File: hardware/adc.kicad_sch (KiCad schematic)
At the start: 15 parts, among them U2 MCP3562R-E/ST

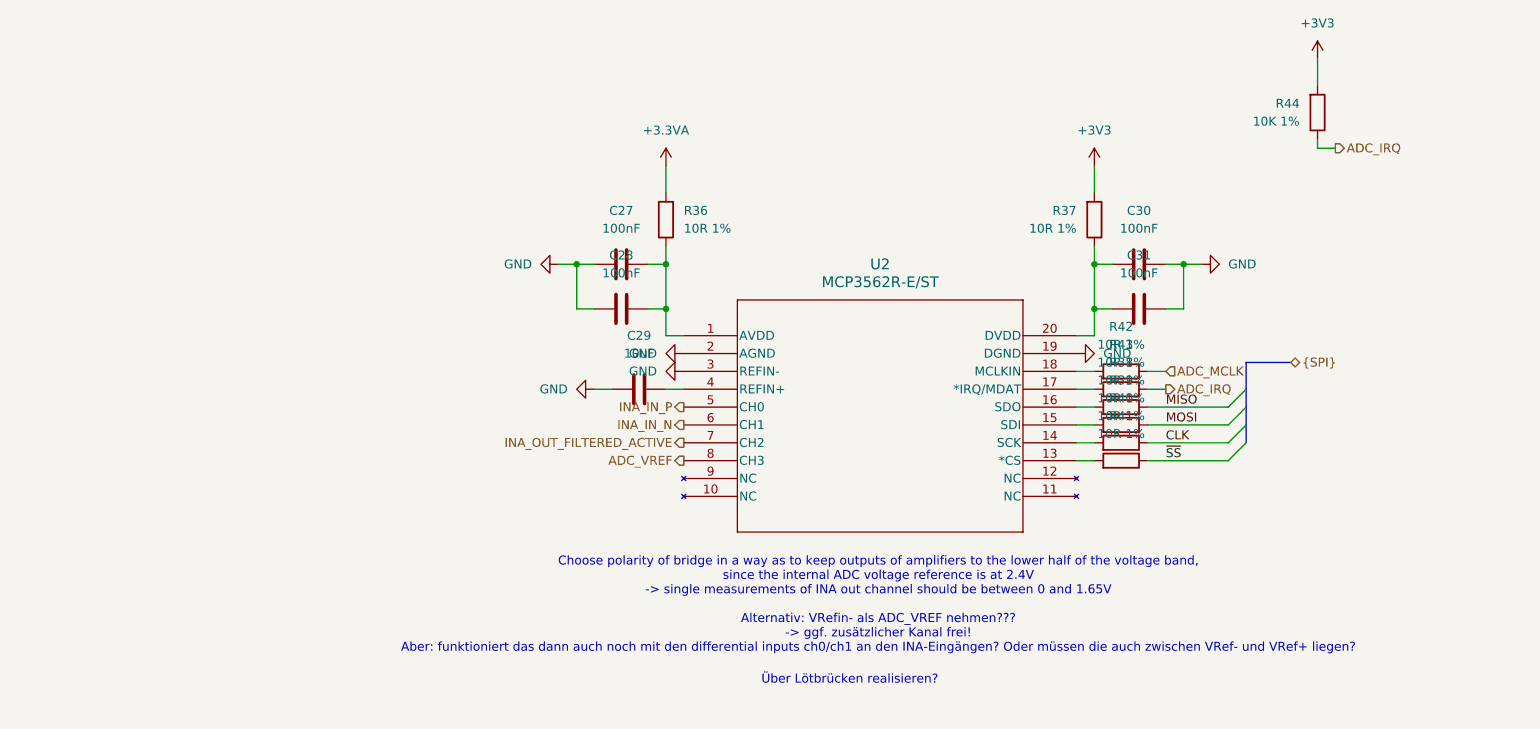
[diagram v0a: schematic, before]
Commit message: Added solder bridges and calculated resistor values for INA
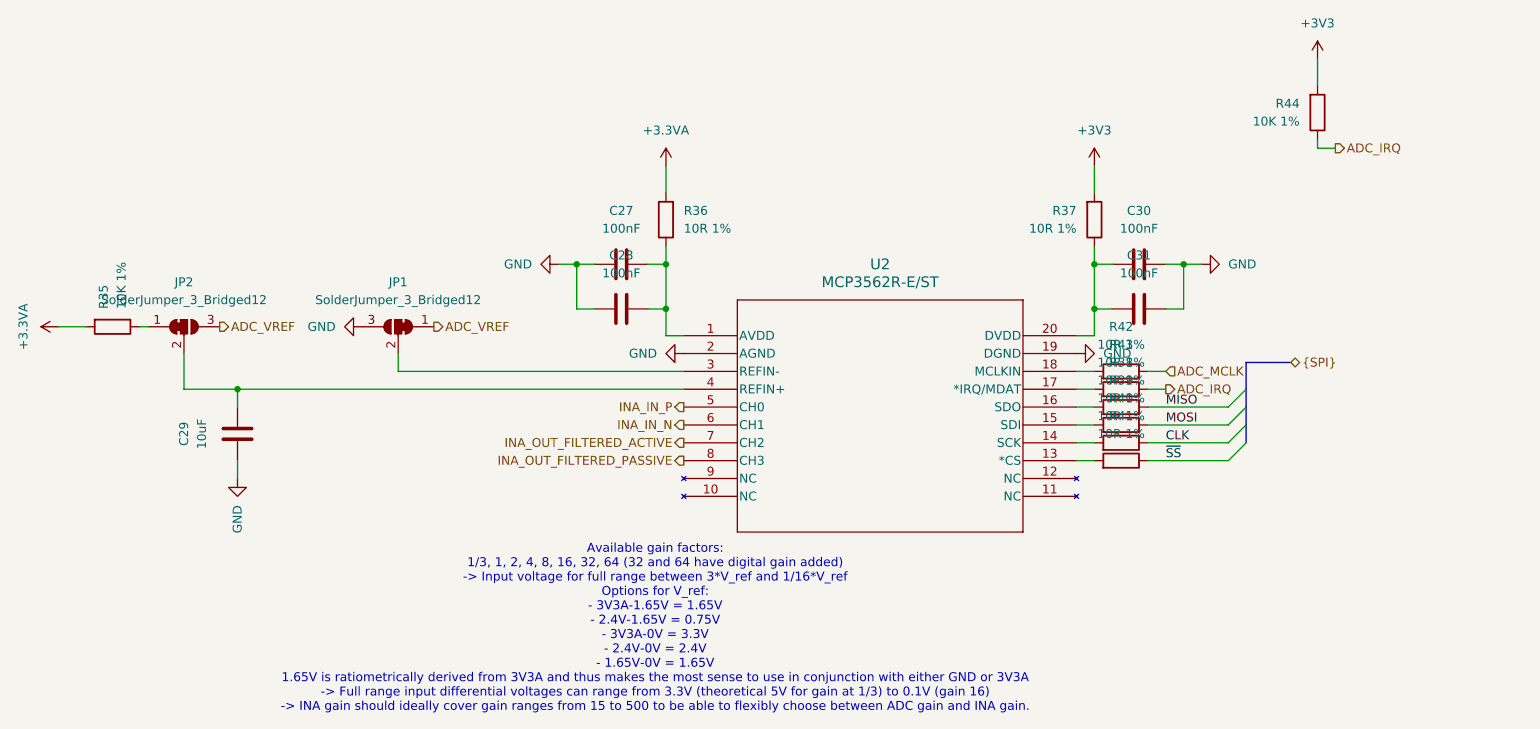
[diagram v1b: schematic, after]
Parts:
- added JP1, JP2: SolderJumper_3_Bridged12, symbol Jumper:SolderJumper_3_Bridged12
- added R35: 10K 1%, Resistor_SMD:R_0603_1608Metric, symbol Device:R
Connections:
- net +3.3VA: now also R35.2
- net ADC_VREF: now also JP1.1 (A), JP2.3 (B); no longer U2.8 (CH3)
- net GND: now also JP1.3 (B); no longer U2.3 (REFIN-)
- net at C29.2, U2.4 (REFIN+): now also JP2.2 (C)
- new net: JP2.1 (A), R35.1
- new net: JP1.2 (C), U2.3 (REFIN-)
- new net INA_OUT_FILTERED_PASSIVE: U2.8 (CH3)
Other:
- note added: "Available gain factors: 1/3, 1, 2, 4, 8, 16, 32, 64 (32 and 64 have digital gain added) -> Input voltage for full range between 3*V_ref and 1/16*V_ref Options for V_ref: - 3V3A-1.65V = 1.65V - 2.4V-1.65V = 0.75V - 3V3A-0V = 3.3V - 2.4V-0V = 2.4V - 1.65V-0V = 1.65V 1.65V is ratiometrically derived from 3V3A and thus makes the most sense to use in conjunction with either GND or 3V3A -> Full range i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"
- note removed: "Choose polarity of bridge in a way as to keep outputs of amplifiers to the lower half of the voltage band, since the internal ADC voltage reference is at 2.4V -> single measurements of INA out channel should be between 0 and 1.65V Alternativ: VRefin- als ADC_VREF nehmen??? -> ggf. zusätzlicher Kanal frei! Aber: funktioniert das dann auch noch mit den differential inputs ch0/ch1 an den INA-Eingäng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"
- note removed: "Über Lötbrücken realisieren?"
- moved on the sheet: C29

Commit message: Set jumper footprints and updated design rules for Oshpark After Dark
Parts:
- JP1, JP2: footprint (none) -> Jumper:SolderJumper-3_P1.3mm_Bridged2Bar12_RoundedPad1.0x1.5mm
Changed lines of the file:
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@@
 			)
 		)
-		(property "Footprint" ""
+		(property "Footprint" "Jumper:SolderJumper-3_P1.3mm_Bridged2Bar12_RoundedPad1.0x1.5mm"
 			(at 36.83 87.63 0)
 			(effects
@@
 			)
 		)
-		(property "Footprint" ""
+		(property "Footprint" "Jumper:SolderJumper-3_P1.3mm_Bridged2Bar12_RoundedPad1.0x1.5mm"
 			(at 67.31 87.63 0)
 			(effects

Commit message: Added net classes
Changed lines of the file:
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@@
+		)
+	)
+	(wire
+		(pts
+			(xy 99.06 101.6) (xy 107.95 101.6)
+		)
+		(stroke
+			(width 0)
+			(type default)
+		)
+	)
+	(wire
+		(pts
+			(xy 99.06 106.68) (xy 107.95 106.68)
+		)
+		(stroke
+			(width 0)
+			(type default)
 		)
 	)
@@
 	(wire
 		(pts
+			(xy 99.06 99.06) (xy 107.95 99.06)
+		)
+		(stroke
+			(width 0)
+			(type default)
+		)
+	)
+	(wire
+		(pts
 			(xy 173.99 99.06) (xy 185.42 99.06)
 		)
@@
 		(pts
 			(xy 166.37 78.74) (xy 166.37 85.09)
+		)
+		(stroke
+			(width 0)
+			(type default)
+		)
+	)
+	(wire
+		(pts
+			(xy 99.06 104.14) (xy 107.95 104.14)
 		)
 		(stroke
@@
 	(hierarchical_label "INA_OUT_FILTERED_PASSIVE"
 		(shape output)
-		(at 107.95 106.68 180)
+		(at 99.06 106.68 180)
 		(effects
 			(font
@@
 	(hierarchical_label "INA_OUT_FILTERED_ACTIVE"
 		(shape output)
-		(at 107.95 104.14 180)
+		(at 99.06 104.14 180)
 		(effects
 			(font
@@
 	(hierarchical_label "INA_IN_P"
 		(shape output)
-		(at 107.95 99.06 180)
+		(at 99.06 99.06 180)
 		(effects
 			(font
@@
 	(hierarchical_label "INA_IN_N"
 		(shape output)
-		(at 107.95 101.6 180)
+		(at 99.06 101.6 180)
 		(effects
 			(font
@@
 		)
 	)
+	(netclass_flag ""
+		(length 2.54)
+		(shape round)
+		(at 165.1 93.98 0)
+		(fields_autoplaced yes)
+		(effects
+			(font
+				(size 1.27 1.27)
+			)
+			(justify left bottom)
+		)
+		(property "Netclass" "Bus"
+			(at 165.7985 91.44 0)
+			(effects
+				(font
+					(size 1.27 1.27)
+				)
+				(justify left)
+			)
+		)
+		(property "Component Class" ""
+			(at -48.26 -3.81 0)
+			(effects
+				(font
+					(size 1.27 1.27)
+					(italic yes)
+				)
+			)
+		)
+	)
+	(netclass_flag ""
+		(length 2.54)
+		(shape round)
+		(at 165.1 99.06 0)
+		(fields_autoplaced yes)
+		(effects
+			(font
+				(size 1.27 1.27)
+			)
+			(justify left bottom)
+		)
+		(property "Netclass" "Bus"
+			(at 165.7985 96.52 0)
+			(effects
+				(font
+					(size 1.27 1.27)
+				)
+				(justify left)
+			)
+		)
+		(property "Component Class" ""
+			(at -48.26 1.27 0)
+			(effects
+				(font
+					(size 1.27 1.27)
+					(italic yes)
+				)
+			)
+		)
+	)
+	(netclass_flag ""
+		(length 2.54)
+		(shape round)
+		(at 165.1 101.6 0)
+		(fields_autoplaced yes)
+		(effects
+			(font
+				(size 1.27 1.27)
+			)
+			(justify left bottom)
+		)
+		(property "Netclass" "Bus"
+			(at 165.7985 99.06 0)
+			(effects
+				(font
+					(size 1.27 1.27)
+				)
+				(justify left)
+			)
+		)
+		(property "Component Class" ""
+			(at -48.26 3.81 0)
+			(effects
+				(font
+					(size 1.27 1.27)
+					(italic yes)
+				)
+			)
+		)
+	)
+	(netclass_flag ""
+		(length 2.54)
+		(shape round)
+		(at 165.1 104.14 0)
+		(fields_autoplaced yes)
+		(effects
+			(font
+				(size 1.27 1.27)
+			)
+			(justify left bottom)
+		)
+		(property "Netclass" "Bus"
+			(at 165.7985 101.6 0)
+			(effects
+				(font
+					(size 1.27 1.27)
+				)
+				(justify left)
+			)
+		)
+		(property "Component Class" ""
+			(at -48.26 6.35 0)
+			(effects
+				(font
+					(size 1.27 1.27)
+					(italic yes)
+				)
+			)
+		)
+	)
